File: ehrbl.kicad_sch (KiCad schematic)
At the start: 104 parts, among them J1 3305-0-15-80-47-27-10-0, J10 3305-0-15-80-47-27-10-0, J11 3305-0-15-80-47-27-10-0, J12 3305-0-15-80-47-27-10-0, J13 3305-0-15-80-47-27-10-0, J14 3305-0-15-80-47-27-10-0, J15 3305-0-15-80-47-27-10-0, J16 3305-0-15-80-47-27-10-0, J17 3305-0-15-80-47-27-10-0, J18 3305-0-15-80-47-27-10-0, J19 3305-0-15-80-47-27-10-0, J2 3305-0-15-80-47-27-10-0, J20 3305-0-15-80-47-27-10-0, J21 3305-0-15-80-47-27-10-0, J22 3305-0-15-80-47-27-10-0, J23 3305-0-15-80-47-27-10-0, J24 3305-0-15-80-47-27-10-0, J25 3305-0-15-80-47-27-10-0, J26 3305-0-15-80-47-27-10-0, J27 3305-0-15-80-47-27-10-0, J28 3305-0-15-80-47-27-10-0, J29 3305-0-15-80-47-27-10-0, J3 3305-0-15-80-47-27-10-0, J30 3305-0-15-80-47-27-10-0, J31 3305-0-15-80-47-27-10-0, J32 3305-0-15-80-47-27-10-0, J33 3305-0-15-80-47-27-10-0, J34 3305-0-15-80-47-27-10-0, J35 3305-0-15-80-47-27-10-0, J36 3305-0-15-80-47-27-10-0, J37 3305-0-15-80-47-27-10-0, J38 3305-0-15-80-47-27-10-0, J39 3305-0-15-80-47-27-10-0, J4 3305-0-15-80-47-27-10-0, J40 3305-0-15-80-47-27-10-0, J41 3305-0-15-80-47-27-10-0, J42 3305-0-15-80-47-27-10-0, J43 3305-0-15-80-47-27-10-0, J44 3305-0-15-80-47-27-10-0, J45 3305-0-15-80-47-27-10-0, J46 3305-0-15-80-47-27-10-0, J47 3305-0-15-80-47-27-10-0, J48 3305-0-15-80-47-27-10-0, J49 3305-0-15-80-47-27-10-0, J5 3305-0-15-80-47-27-10-0, J50 3305-0-15-80-47-27-10-0, J51 3305-0-15-80-47-27-10-0, J52 3305-0-15-80-47-27-10-0, J53 MF254V-11-07-0743, J54 MF254V-11-07-0743, J55 MF254V-11-07-0743, J56 MF254V-11-07-0743, J57 0906, J58 0906, J6 3305-0-15-80-47-27-10-0, J7 3305-0-15-80-47-27-10-0, J8 3305-0-15-80-47-27-10-0, J9 3305-0-15-80-47-27-10-0, SW1 SW_Push, SW10 SW_Push, SW11 SW_Push, SW12 SW_Push, SW13 SW_Push, SW14 SW_Push, SW15 SW_Push, SW16 SW_Push, SW17 SW_Push, SW18 SW_Push, SW19 SW_Push, SW2 SW_Push, SW20 SW_Push, SW21 SW_Push, SW22 SW_Push, SW23 SW_Push, SW24 SW_Push, SW25 SW_Push, SW26 SW_Push, SW27 RotaryEncoder_Switch, SW28 RotaryEncoder_Switch, SW29 SSSS811101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

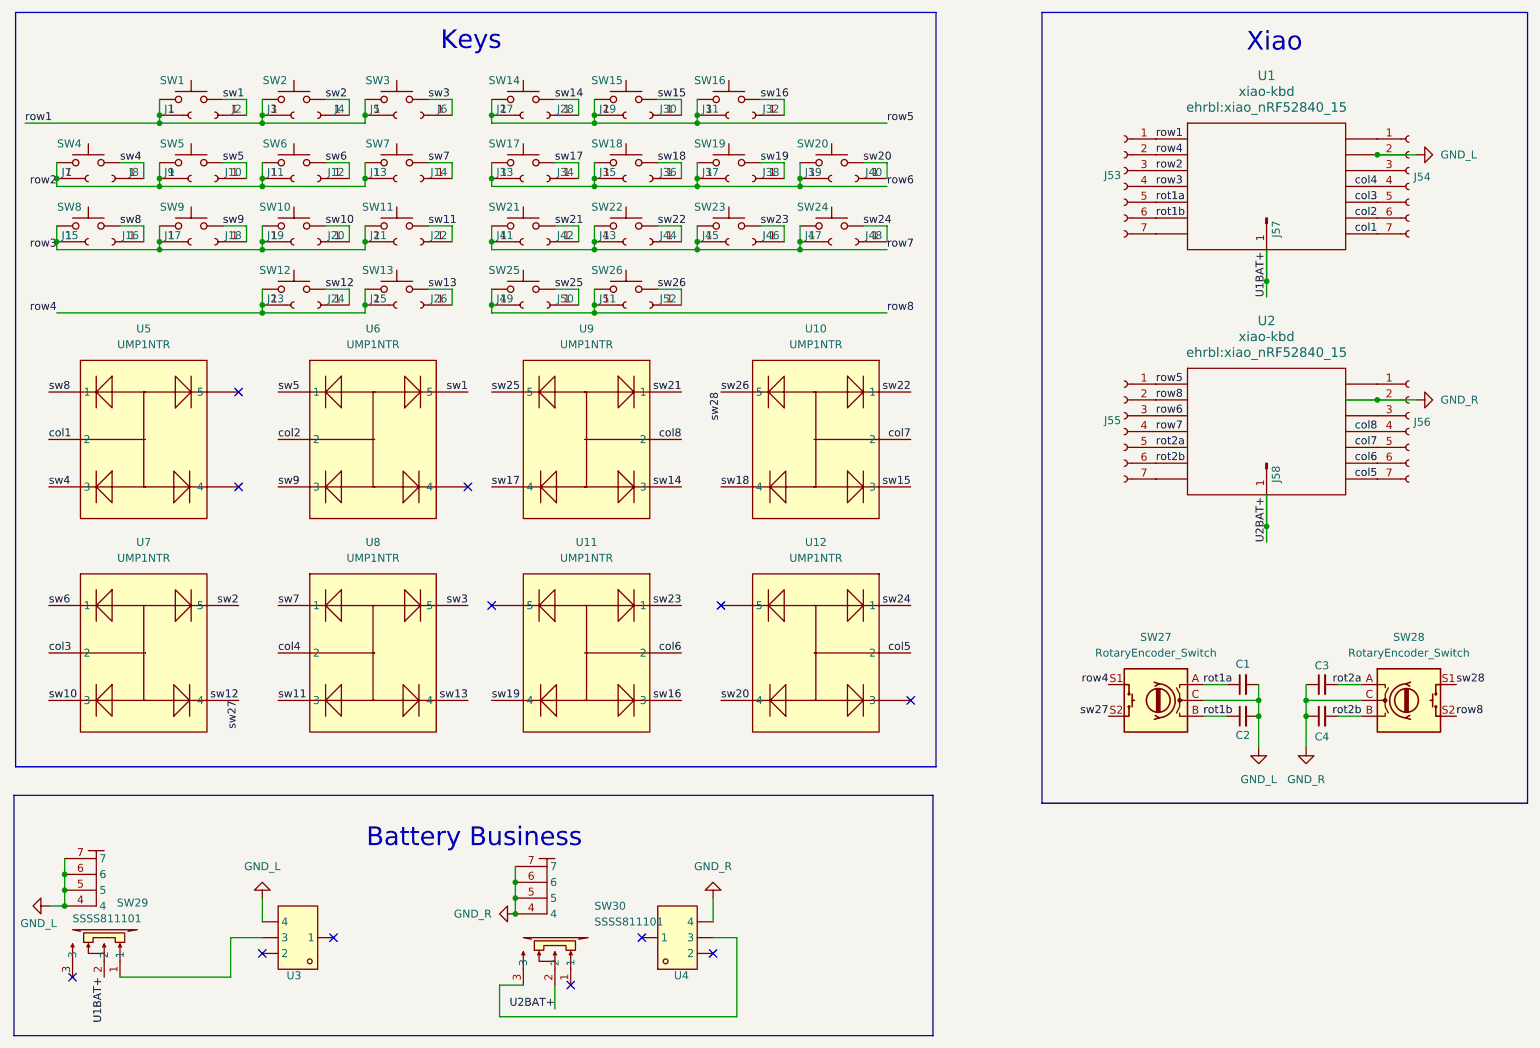
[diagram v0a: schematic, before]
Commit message: back to 28 keys
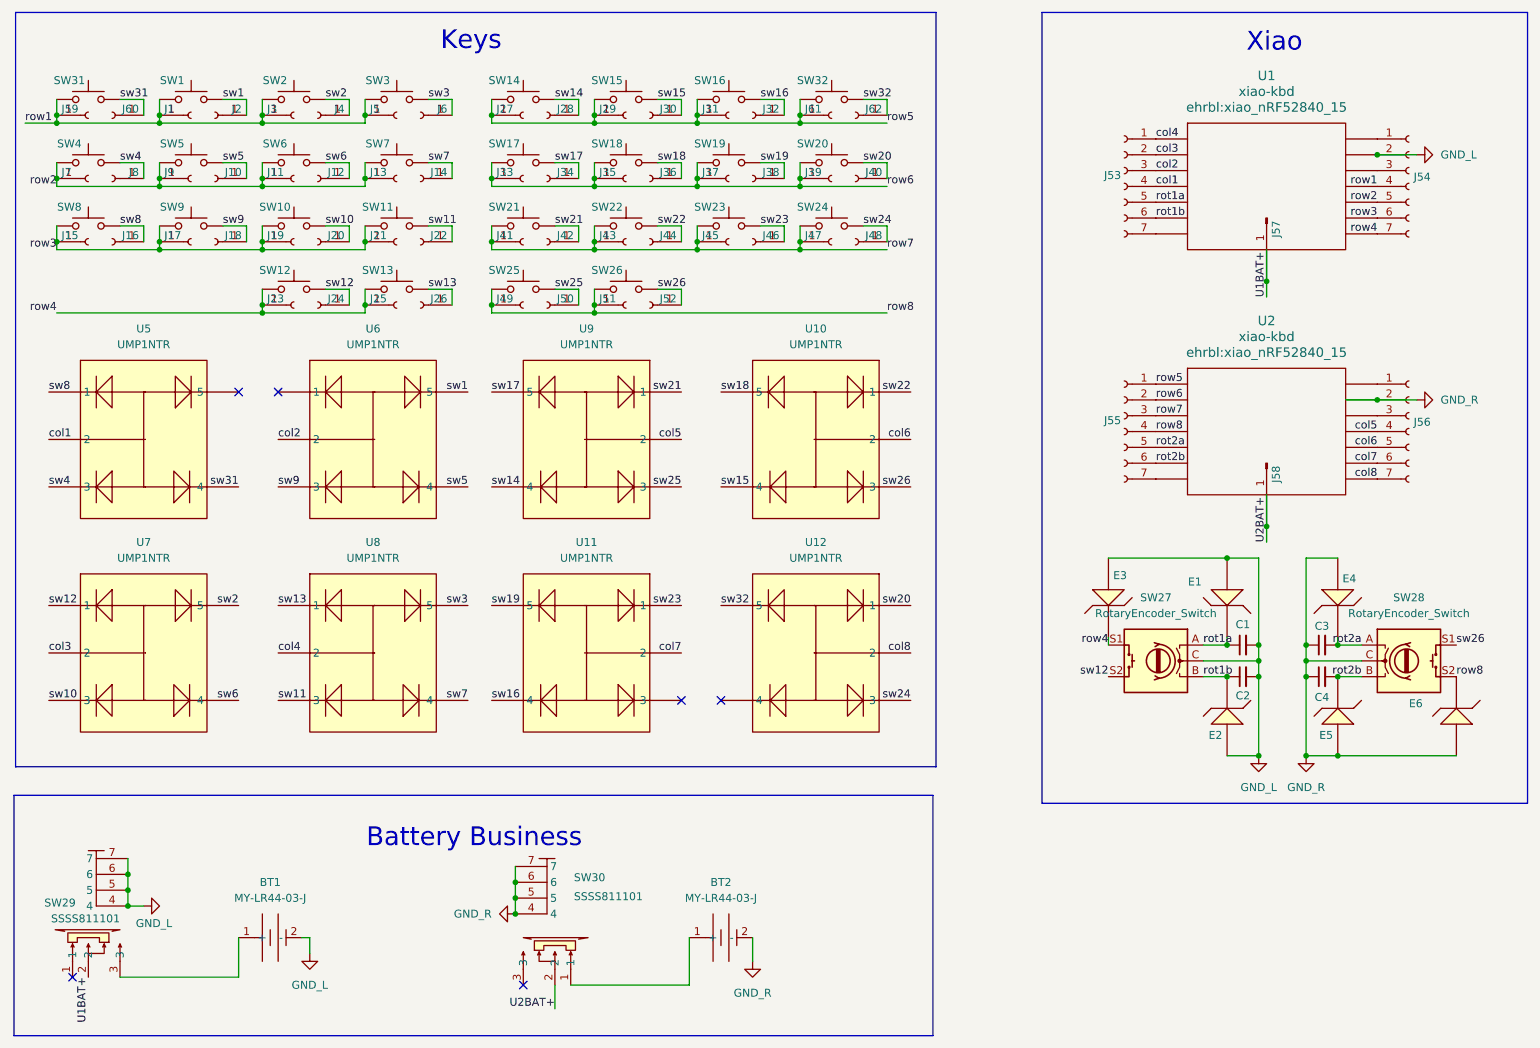
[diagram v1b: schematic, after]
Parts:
- removed U3, U4: MY-LR44-02, ehrbl:BAT-SMD_MY-LR44-02, symbol ehrbl:MY-LR44-02
- added BT1, BT2: MY-LR44-03-J, ehrbl:CONN-TH_MY-LR44-03-J, symbol ehrbl:MY-LR44-03-J
- added E1, E2, E3, E4, E5, E6: CESD5V0D3 ZA, ehrbl:SOD-323_L1.8-W1.3-LS2.5-RD, symbol ehrbl:CESD5V0D3ZA
- added J59, J60, J61, J62: 3305-0-15-80-47-27-10-0, ehrbl:3305-0-15-80-47-27-10-0, symbol Connector:Conn_01x01_Socket
- added SW31, SW32: SW_Push, ehrbl:SW_PG1350, symbol Switch:SW_Push
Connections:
- net GND_L: now also BT1.2 (-), E1.2, E2.2, E3.2
- net GND_R: now also BT2.2 (-), E4.2, E5.2, E6.2
- net col1: now also J53.4 (Pin_4), U1.4 (D3); no longer J54.7 (Pin_7), U1.8 (D7)
- net col2: now also J53.3 (Pin_3), U1.3 (D2); no longer J54.6 (Pin_6), U1.9 (D8)
- net col3: now also J53.2 (Pin_2), U1.2 (D1); no longer J54.5 (Pin_5), U1.10 (D9)
- net col4: now also J53.1 (Pin_1), U1.1 (D0); no longer J54.4 (Pin_4), U1.11 (D10)
- net col5: now also J56.4 (Pin_4), U2.11 (D10), U9.2; no longer J56.7 (Pin_7), U12.2, U2.8 (D7)
- net col6: now also J56.5 (Pin_5), U10.2, U2.10 (D9); no longer J56.6 (Pin_6), U11.2, U2.9 (D8)
- net col7: now also J56.6 (Pin_6), U11.2, U2.9 (D8); no longer J56.5 (Pin_5), U10.2, U2.10 (D9)
- net col8: now also J56.7 (Pin_7), U12.2, U2.8 (D7); no longer J56.4 (Pin_4), U2.11 (D10), U9.2
- net rot1a: now also E1.1
- net rot1b: now also E2.1
- net rot2a: now also E4.1
- net rot2b: now also E5.1
- net row1: now also J54.4 (Pin_4), U1.11 (D10), J59.1 (Pin_1), SW31.1; no longer J53.1 (Pin_1), U1.1 (D0)
- net row2: now also J54.5 (Pin_5), U1.10 (D9); no longer J53.3 (Pin_3), U1.3 (D2)
- net row3: now also J54.6 (Pin_6), U1.9 (D8); no longer J53.4 (Pin_4), U1.4 (D3)
- net row4: now also J54.7 (Pin_7), U1.8 (D7), E3.1; no longer J53.2 (Pin_2), U1.2 (D1)
- net row5: now also J61.1 (Pin_1), SW32.1
- net row6: now also J55.2 (Pin_2), U2.2 (D1); no longer J55.3 (Pin_3), U2.3 (D2)
- net row7: now also J55.3 (Pin_3), U2.3 (D2); no longer J55.4 (Pin_4), U2.4 (D3)
- net row8: now also J55.4 (Pin_4), U2.4 (D3), E6.1; no longer J55.2 (Pin_2), U2.2 (D1)
- net sw12: now also U7.1; no longer U7.4
- net sw13: now also U8.1; no longer U8.4
- net sw14: now also U9.4; no longer U9.3
- net sw15: now also U10.4; no longer U10.3
- net sw16: now also U11.4; no longer U11.3
- net sw17: now also U9.5; no longer U9.4
- net sw18: now also U10.5; no longer U10.4
- net sw19: now also U11.5; no longer U11.4
- net sw20: now also U12.1; no longer U12.4
- net sw24: now also U12.3; no longer U12.1
- net sw25: now also U9.3; no longer U9.5
- net sw26: now also U10.3; no longer U10.5
- net sw5: now also U6.4; no longer U6.1
- net sw6: now also U7.4; no longer U7.1
- net sw7: now also U8.4; no longer U8.1
- net at SW29.3: now also BT1.1 (+)
- net sw32: now reaches U12.5
- net sw32: now also J62.1 (Pin_1), SW32.2
- net sw31: now reaches U5.4
- net sw31: now also J60.1 (Pin_1), SW31.2
- net at SW30.1: now also BT2.1 (+)
- no-connect marks 12 -> 6
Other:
- moved on the sheet: C1, C2, C3, C4, SW27, SW28, SW29
